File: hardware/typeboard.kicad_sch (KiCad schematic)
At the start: 0 parts

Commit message: :construction: explode saki
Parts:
- added PC1, PC2: ~, KeysDock:POGOPIN-8P-HR, symbol components:POGOPIN-8P-HR
- added U1: ~, KeysDock:TLA2528, symbol components:TLA2528
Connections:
- net keys-group-1/KEYS_ADC_OUT: now also U1.15 (AIN0/GPIO0)
- net keys-group-2/KEYS_ADC_OUT: now also U1.16 (AIN1/GPIO1)
- net keys-group-3/KEYS_ADC_OUT: now also U1.1 (AIN2/GPIO2)
- net keys-group-4/KEYS_ADC_OUT: now also U1.2 (AIN3/GPIO3)
- new net: PC1.1 (Y1), U1.3 (AIN4/GPIO4)
- new net KEYS_SCAN_A: PC1.5 (Y5)
- new net KEYS_SCAN_B: PC1.6 (Y6)
- new net KEYS_SCAN_C: PC1.7 (Y7)
- new net KEYS_SCAN_CE: PC1.3 (Y3)
- new net KEYS_SCAN_D: PC1.8 (Y8)
- new net P,+3.3: PC2.3 (Y3)
- new net P,+5: PC2.1 (Y1)
- new net P,E: PC1.2 (Y2), PC1.4 (Y4), PC2.2 (Y2), PC2.4 (Y4), PC2.6 (Y6), U1.17 (GND)
- new net RANA: PC2.7 (Y7)
- new net SAKI_MOVE: PC2.5 (Y5)
- new net keys-group-4/TOMO0_OUT: PC2.8 (Y8)
- no-connect marks 1 -> 0
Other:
- sheet keys-group-1 ports: added TOMO0_IN, TOMO0_OUT; removed LED_DATA_IN, LED_DATA_OUT
- sheet keys-group-2 ports: added TOMO0_IN, TOMO0_OUT; removed LED_DATA_IN, LED_DATA_OUT
- sheet keys-group-3 ports: added TOMO0_IN, TOMO0_OUT; removed LED_DATA_IN, LED_DATA_OUT
- sheet keys-group-4 ports: added TOMO0_IN, TOMO0_OUT; removed LED_DATA_IN, LED_DATA_OUT

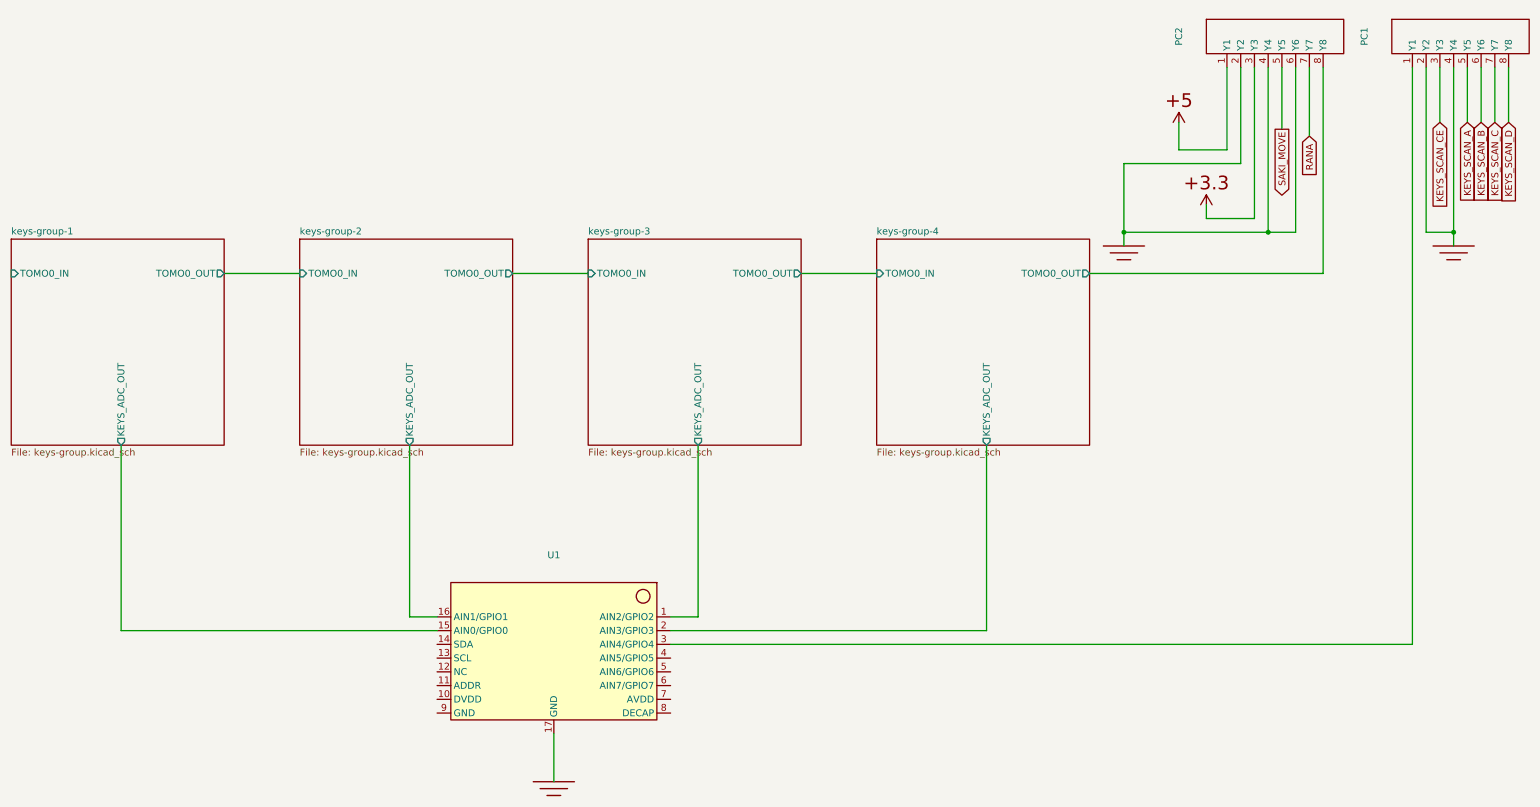
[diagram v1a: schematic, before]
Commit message: :fire: remove external adc, use internal adc io pins
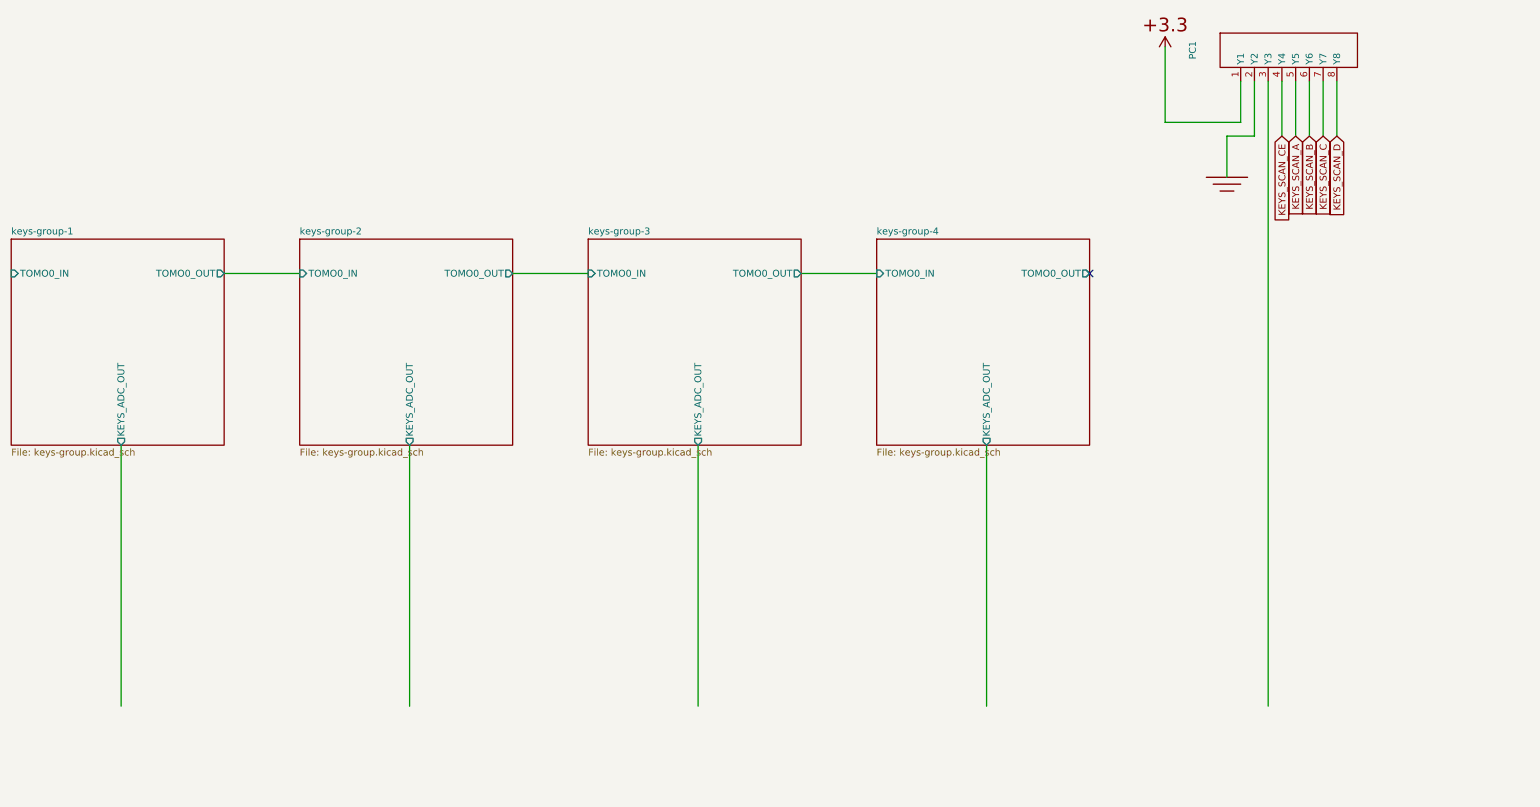
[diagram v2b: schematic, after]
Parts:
- removed PC2: ~, KeysDock:POGOPIN-8P-HR, symbol components:POGOPIN-8P-HR
- removed U1: ~, KeysDock:TLA2528, symbol components:TLA2528
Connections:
- net KEYS_SCAN_CE: now also PC1.4 (Y4); no longer PC1.3 (Y3)
- net P,+3.3: now also PC1.1 (Y1)
- net P,E: no longer PC1.4 (Y4)
- no-connect marks 0 -> 1
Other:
- moved on the sheet: PC1
